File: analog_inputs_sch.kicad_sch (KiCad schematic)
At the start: 16 parts, among them J1 Conn_Coaxial, K1 Relay_SPDT, K2 Relay_SPDT, K3 Relay_SPDT, U1 OPA656U, U2 AD8045ACPZ-R2, U6 LTC2299xUP, U7 LMH6551MA

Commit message: First schematic version of AF
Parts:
- removed R4, R5, R6, R7: R, symbol Device:R
- removed U2: AD8045ACPZ-R2, CP_8_2_ADI, symbol 2025-07-01_23-44-10:AD8045ACPZ-R2
- removed U6: LTC2299xUP, Package_DFN_QFN:QFN-64-1EP_9x9mm_P0.5mm_EP7.15x7.15mm, symbol Analog_ADC:LTC2299xUP
- removed U7: LMH6551MA, Package_SO:SOIC-8_3.9x4.9mm_P1.27mm, symbol Amplifier_Operational:LMH6551MA
- added C10: C, symbol Device:C
- added C2, C7: C 360 pF, symbol Device:C
- added C3, C5, C6, C9: C 2.0 - 6.0 pF, symbol Device:C_Variable
- added C4, C8: C 390 pF, symbol Device:C
- added J2: Conn_Coaxial, symbol Connector:Conn_Coaxial
- added K4, K5, K6: Relay_SPDT, symbol Relay:Relay_SPDT
- added R10, R14: R 49.9k, symbol Device:R
- added R11, R15, R8: R 953k, symbol Device:R
- added R12, R9: R 47k, symbol Device:R
- added R13, R16: R, symbol Device:R
- added U8: OPA656U, OPA656U:SOIC127P599X175-8N, symbol OPA656U:OPA656U
- R3: value R -> R 953k
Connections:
- net GND: now also C2.2, C3.2, C7.2, C9.2, J2.2 (Ext), R11.2, R12.2, R15.2, R9.2; no longer R3.2
- net at C1.1, K3.12, R2.2: no longer R3.1
- net at K1.12: now also C4.1, R10.1; no longer K2.12
- net at K1.14: now also C6.1, R8.1
- net at K2.11, R2.1: no longer K2.A2
- net CH1_VGA: now reaches U1.2 (NEG), U1.6 (OUTPUT)
- net at K2.14: now also C2.1, C6.2, R8.2, R9.1
- new net: C5.2, C7.1, K5.14, R12.1, R3.2
- new net: J2.1 (In), R13.1
- new net: K5.11, R16.1
- new net: C10.1, K6.12, R16.2
- new net: C3.1, C4.2, K2.12, R10.2, R11.1
- new net: C10.2, K6.11, U8.3 (POS)
- new net: C8.1, K4.12, R14.1
- new net: C8.2, C9.1, K5.12, R14.2, R15.1
- new net: K4.11, R13.2
- new net: C5.1, K4.14, R3.1
- new net CH2_VGA: U8.2 (NEG), U8.6 (OUTPUT)
- no-connect marks 1 -> 2
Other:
- note added: "1 : 21.27"
- note added: "1:1"
- note added: "AC / DC"
- note added: "CH2"
- note added: "FET buffer"
- note added: "V < 500 mV / div"
- note added: "V > 500mV / div"
- moved on the sheet: C1, J1, K1, K2, K3, R1, R2, U1

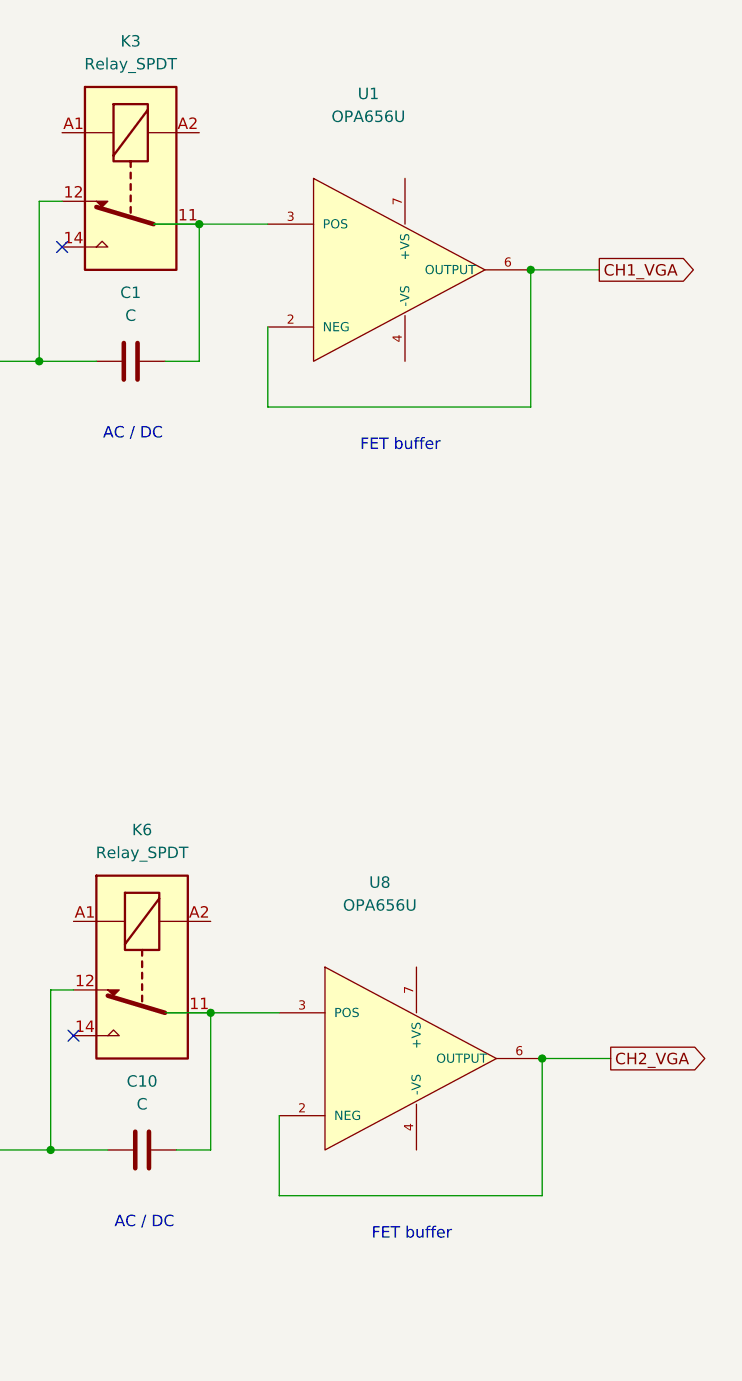
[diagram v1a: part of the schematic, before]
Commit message: Chose amplifiers
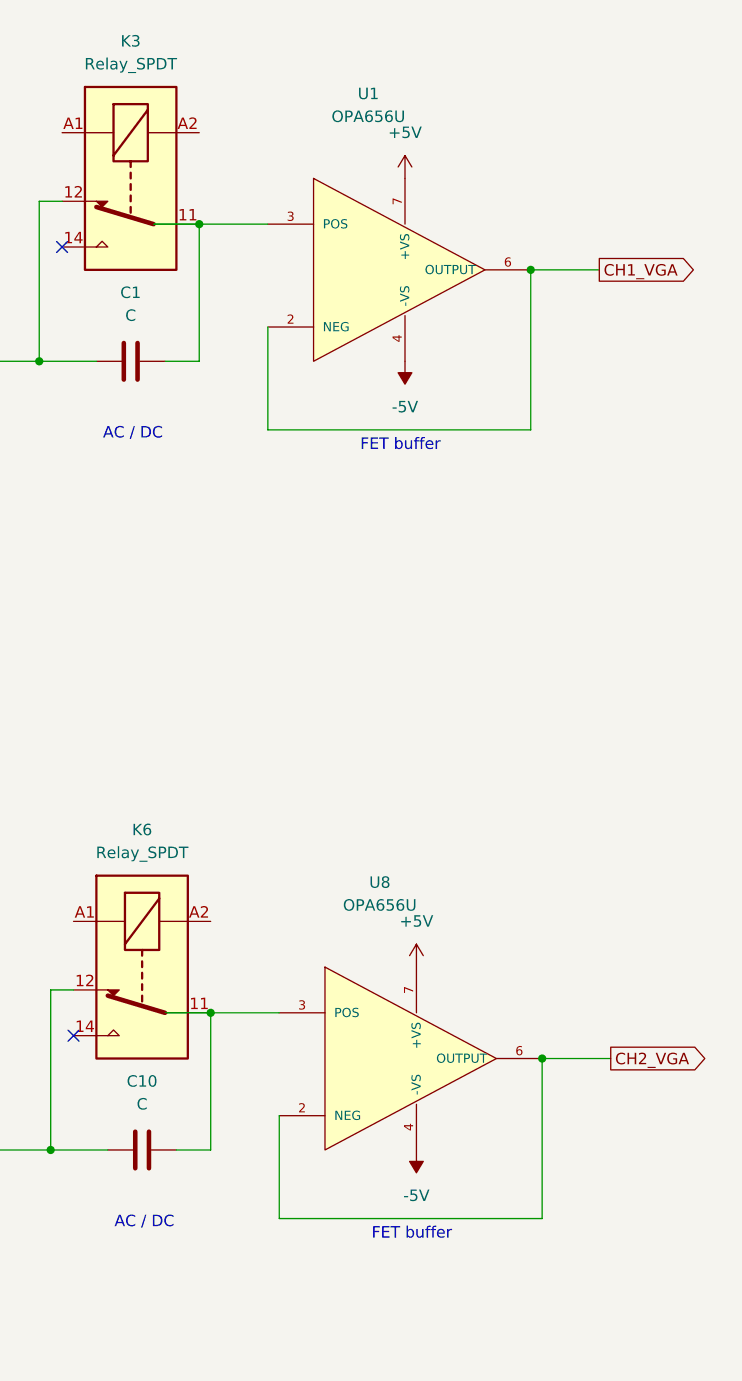
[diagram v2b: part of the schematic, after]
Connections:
- net -5V: now reaches U8.4 (-VS)
- net -5V: now also U1.4 (-VS)
- net +5V: now reaches U8.7 (+VS)
- net +5V: now also U1.7 (+VS)

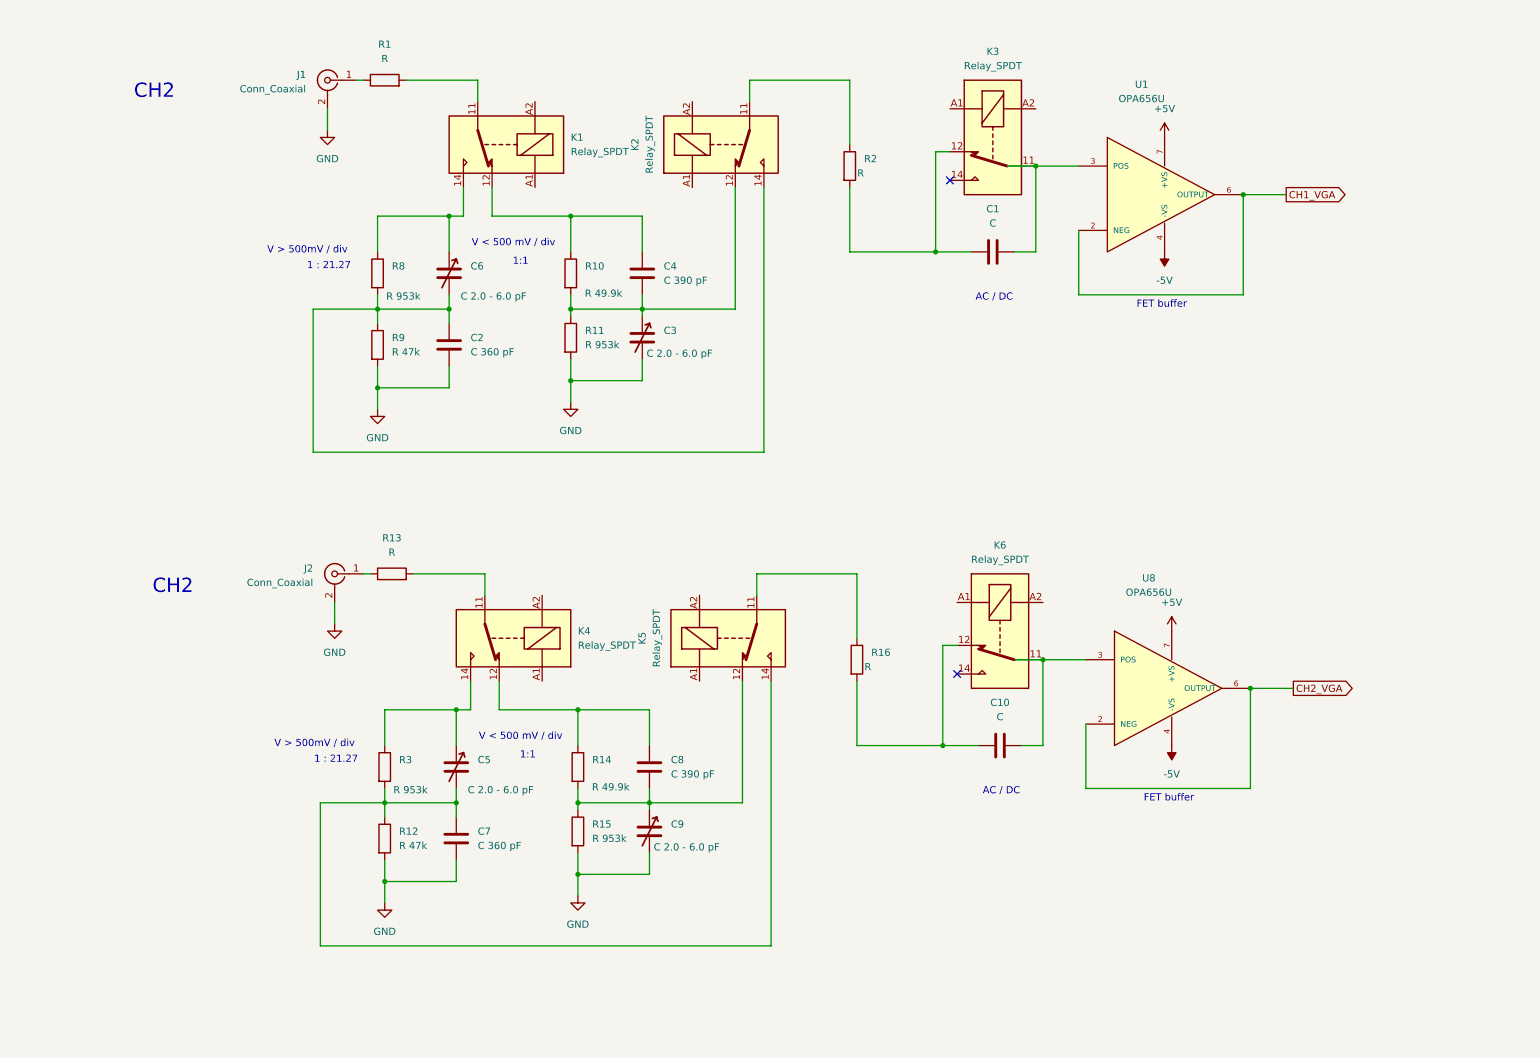
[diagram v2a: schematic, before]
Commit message: Move the trigger
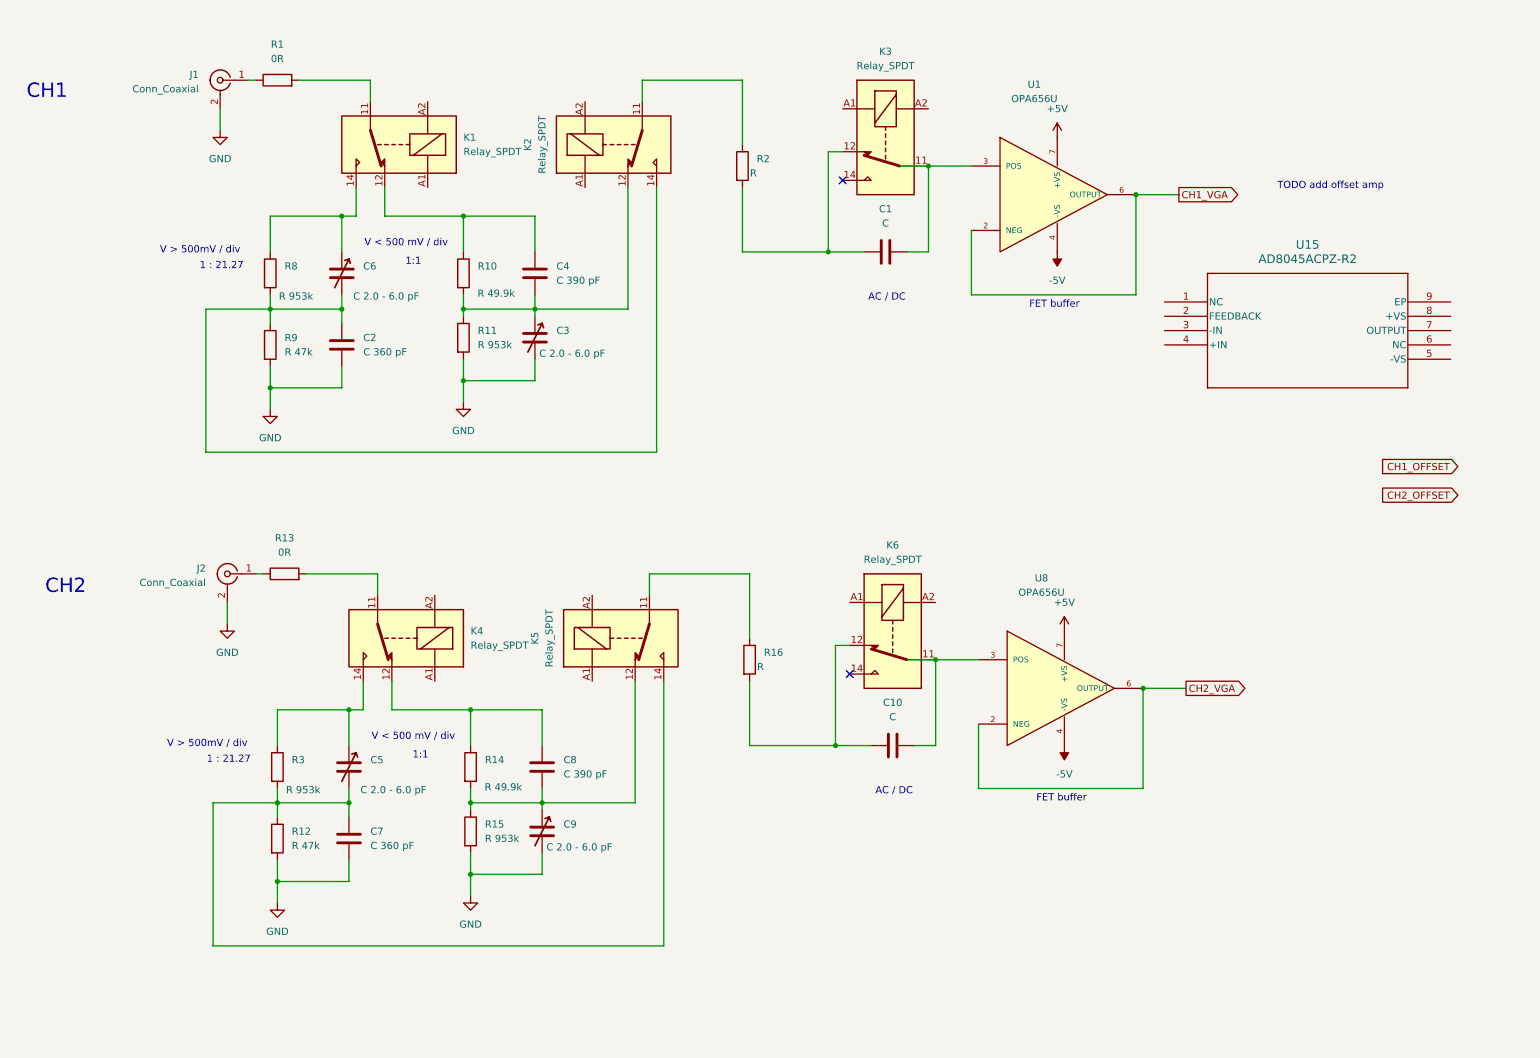
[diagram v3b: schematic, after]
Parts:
- added U15: AD8045ACPZ-R2, CP_8_2_ADI, symbol 2025-07-01_23-44-10:AD8045ACPZ-R2
- R1, R13: value R -> 0R
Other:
- note added: "CH1"
- note added: "TODO add offset amp"
- moved on the sheet: C1, C10, C2, C3, C4, C5, C6, C7, C8, C9, J1, J2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

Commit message: First version of analog path, without resistor values
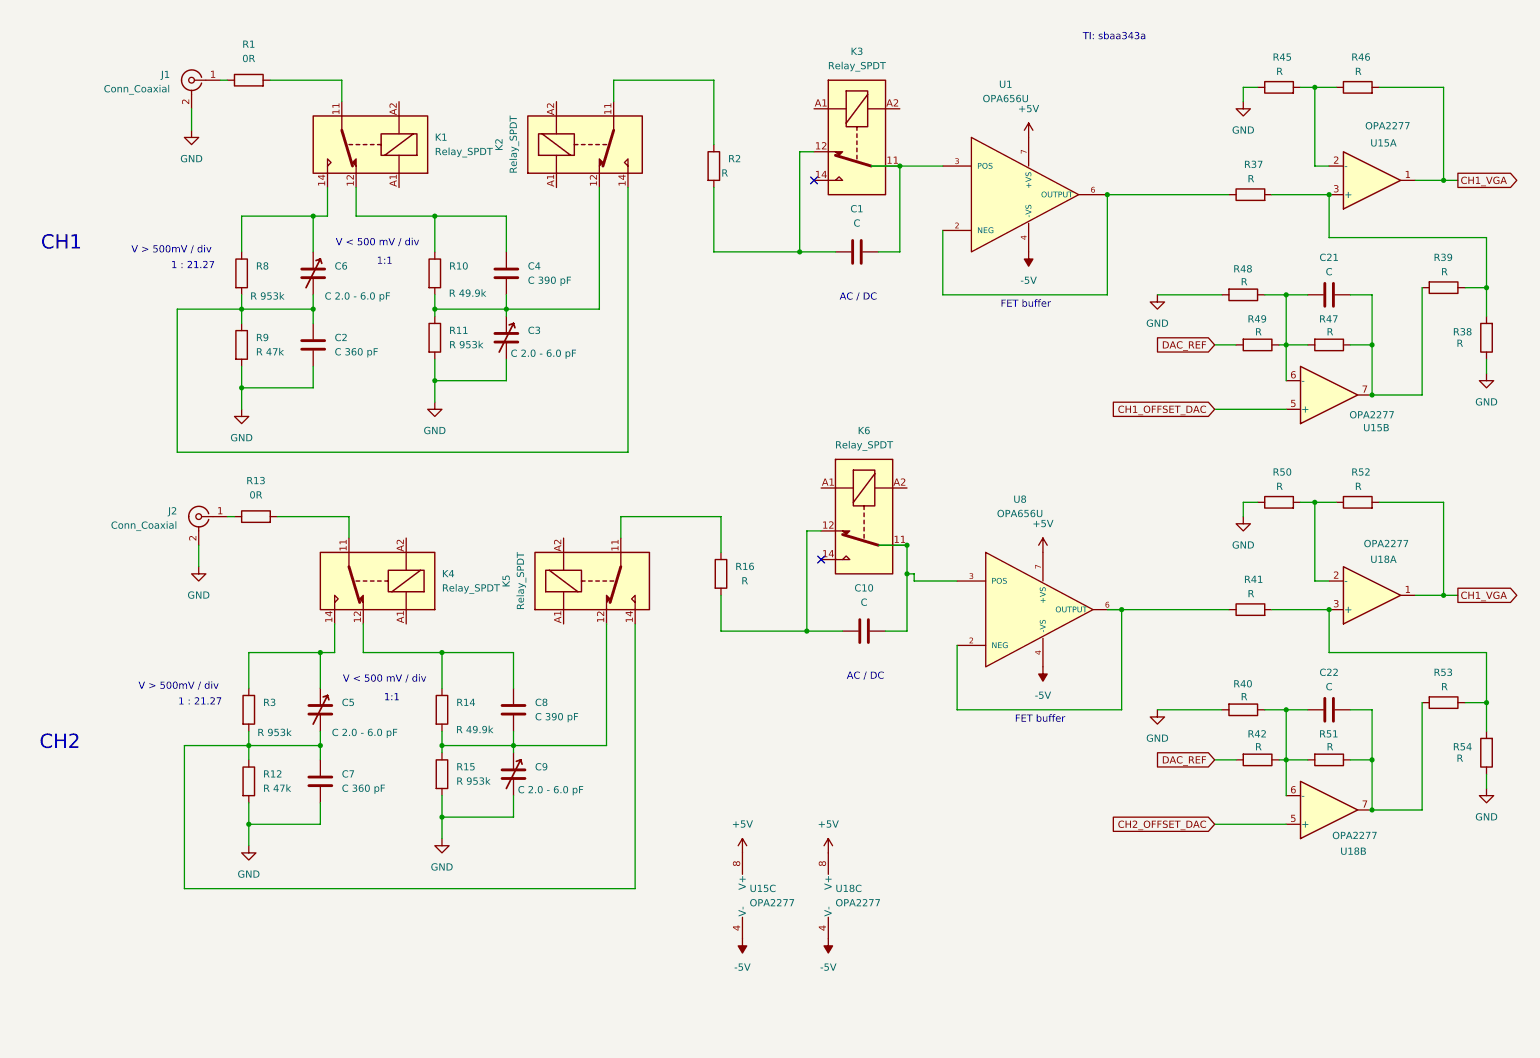
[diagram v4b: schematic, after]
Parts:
- removed U15: AD8045ACPZ-R2, CP_8_2_ADI, symbol 2025-07-01_23-44-10:AD8045ACPZ-R2
- added C21, C22: C, symbol Device:C
- added R37, R38, R39, R40, R41, R42, R45, R46, R47, R48, R49, R50, R51, R52, R53, R54: R, symbol Device:R
- added U15, U18: OPA2277, symbol Amplifier_Operational:OPA2277
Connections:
- net +5V: now also U15.8 (V+), U18.8 (V+)
- net -5V: now also U15.4 (V-), U18.4 (V-)
- net CH1_VGA: now also R46.2, R52.2, U15.1, U18.1; no longer U1.2 (NEG), U1.6 (OUTPUT)
- net GND: now also R38.1, R40.2, R45.1, R48.2, R50.1, R54.1
- net CH2_VGA: no longer names the net of U8.2 (NEG), U8.6 (OUTPUT)
- net CH2_VGA: now also R41.1
- new net: R41.2, R53.1, R54.2, U18.3 (+)
- new net: R37.2, R38.2, R39.1, U15.3 (+)
- new net: R45.2, R46.1, U15.2 (-)
- new net: C22.2, R51.1, R53.2, U18.7
- new net: C21.1, R47.2, R48.1, R49.1, U15.6 (-)
- new net: C21.2, R39.2, R47.1, U15.7
- new net: R50.2, R52.1, U18.2 (-)
- new net: R37.1, U1.2 (NEG), U1.6 (OUTPUT)
- new net: C22.1, R40.1, R42.1, R51.2, U18.6 (-)
- new net CH1_OFFSET_DAC: U15.5 (+)
- new net CH2_OFFSET_DAC: U18.5 (+)
- new net DAC_REF: R42.2, R49.2
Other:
- note added: "TI: sbaa343a"
- note removed: "TODO add offset amp"
- moved on the sheet: C1, C10, C2, C3, C4, C5, C6, C7, C8, C9, J1, J2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
